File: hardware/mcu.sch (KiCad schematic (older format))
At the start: 51 parts, among them P3 CONN_01X08_DEBUG, P4 CONN_02X05_JTAG, P5 CONN_01X03_UART, P6 CONN_01X03_CAN, P7 CONN_01X05_ENCODER, SW2 SW_PUSH, U13 TM4C1294KCPDT, U14 74LVCH2T45, U15 SN65HVD231D, Y1 NX5032GA

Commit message: Gate driver layout mostly complete
- Gate driver layout
- Switch LM5102 for UCC27211 (higher current, more robust)
- Tweak gate drive circuit passives
- No soldermask on high-current traces
- Fix error in orientation of LAH-100P footprint
- Improved draft layout of control section
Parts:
- added C79: 1u, Capacitors_SMD:C_0603, symbol C
- added W22, W23: TEST_1P, symbol TEST_1P
- C32, C33: footprint Capacitors_SMD:C_0603 -> Capacitors_SMD:C_0805
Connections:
- net labels added: AIN_13, AIN_15, AIN_19, M0PWM0, T5CCP0
- net labels removed: AIN_0, AIN_3, GNDA, PWM6, PWM7
- wire segments 199 -> 197
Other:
- note added: "CONNECT JUMPER FOR\nFACTORY RESET ON\nNEXT SYSTEM RESET"
- note removed: "CONNECT TO ENABLE\nFACTORY RESET ON\nNEXT SYSTEM RESET"
- moved on the sheet: JP1, P5, R33, R57, R58, SW2, U13B

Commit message: All routing finished
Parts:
- removed P3: CONN_01X08_DEBUG, Pin_Headers:Pin_Header_Straight_1x08, symbol CONN_01X08
- added P3: CONN_01X09, Pin_Headers:Pin_Header_Straight_1x09, symbol CONN_01X09
- U14: footprint 2kwMotorController:VSSOP8 -> Housings_SSOP:MSOP-8_3x3mm_Pitch0.65mm
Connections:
- net labels added: VDDC
- wire segments 197 -> 200
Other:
- note removed: "REMOVE TO \nSET CAN ID"
- moved on the sheet: C32, C33, C34, C35, C36, C37, C38, C39, C40, C41, C42, C43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

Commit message: All DRC/ERC passed
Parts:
- removed W22, W23: TEST_1P, symbol TEST_1P
- added TP19, TP20, TP21, TP22, TP23: TEST_POINT, 2kwMotorController:TEST_PAD_1.27mm, symbol TEST_POINT
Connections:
- net CANH: now also TP21.1
- net CANL: now also TP22.1
- net CAN_RX: now also TP20.1
- net CAN_TX: now also TP19.1
- net VDDC: now also TP23.1

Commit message: tweaks, testpoints, decluttering
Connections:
- net FRST: now reaches JP1.1, U13.74 (PM4)
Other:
- moved on the sheet: JP1
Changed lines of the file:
@@
 L Jumper_NO_Small JP1
 U 1 1 59C1D74D
-P 5850 2300
-F 0 "JP1" H 5850 2380 50  0000 C CNN
-F 1 "Jumper_NO_Small" H 5860 2240 50  0001 C CNN
-F 2 "Pin_Headers:Pin_Header_Straight_1x02" H 5850 2300 50  0001 C CNN
-F 3 "" H 5850 2300 50  0000 C CNN
-	1    5850 2300
+P 4975 2300
+F 0 "JP1" H 4975 2380 50  0000 C CNN
+F 1 "Jumper_NO_Small" H 4985 2240 50  0001 C CNN
+F 2 "Pin_Headers:Pin_Header_Straight_1x02" H 4975 2300 50  0001 C CNN
+F 3 "" H 4975 2300 50  0000 C CNN
+	1    4975 2300
 	-1   0    0    -1
 $EndComp
@@
 L GND #PWR091
 U 1 1 59C1E162
-P 5700 2350
-F 0 "#PWR091" H 5700 2100 50  0001 C CNN
-F 1 "GND" H 5700 2200 50  0000 C CNN
-F 2 "" H 5700 2350 50  0000 C CNN
-F 3 "" H 5700 2350 50  0000 C CNN
-	1    5700 2350
+P 4825 2350
+F 0 "#PWR091" H 4825 2100 50  0001 C CNN
+F 1 "GND" H 4825 2200 50  0000 C CNN
+F 2 "" H 4825 2350 50  0000 C CNN
+F 3 "" H 4825 2350 50  0000 C CNN
+	1    4825 2350
 	-1   0    0    -1
 $EndComp
-Text Notes 5600 2550 2    60   ~ 0
+Text Notes 5975 2575 2    60   ~ 0
 CONNECT JUMPER FOR\nFACTORY RESET ON\nNEXT SYSTEM RESET
 $Comp
@@
 	8250 2700 8250 2650
 Wire Wire Line
-	8500 2700 8500 2650
+	8500 2650 8500 2700
 Connection ~ 8500 2650
 Wire Wire Line
-	8750 2700 8750 2650
+	8750 2650 8750 2700
 Connection ~ 8750 2650
 Wire Wire Line
@@
 Connection ~ 8500 3050
 Wire Wire Line
-	9000 2700 9000 2650
+	9000 2650 9000 2700
 Connection ~ 9000 2650
 Wire Wire Line
@@
 	3050 4800 3050 4700
 Wire Wire Line
-	6050 2300 5950 2300
-Wire Wire Line
-	5750 2300 5700 2300
-Wire Wire Line
-	5700 2300 5700 2350
+	6050 2300 5075 2300
+Wire Wire Line
+	4875 2300 4825 2300
+Wire Wire Line
+	4825 2300 4825 2350
 Wire Wire Line
 	4550 5150 4550 5250
@@
 Wire Wire Line
 	7900 2650 9450 2650
+Text Label 5600 2300 0    60   ~ 0
+FRST
 $EndSCHEMATC

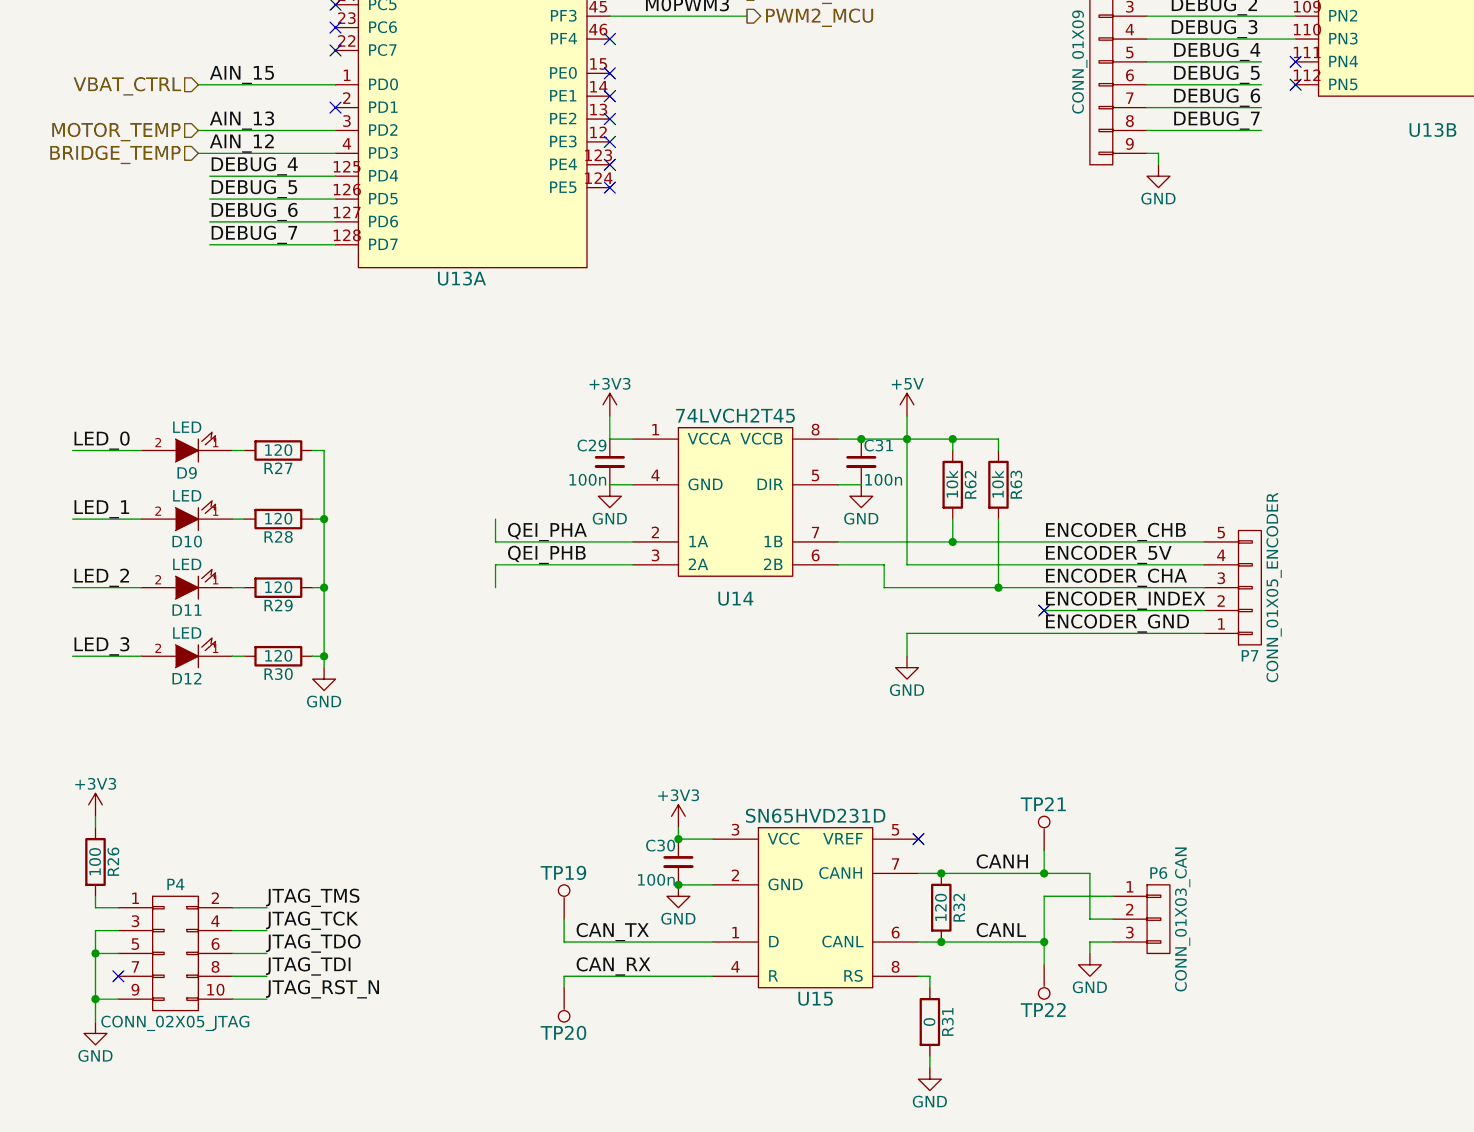
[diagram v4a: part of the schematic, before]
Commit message: Create and verify full Digikey BOM
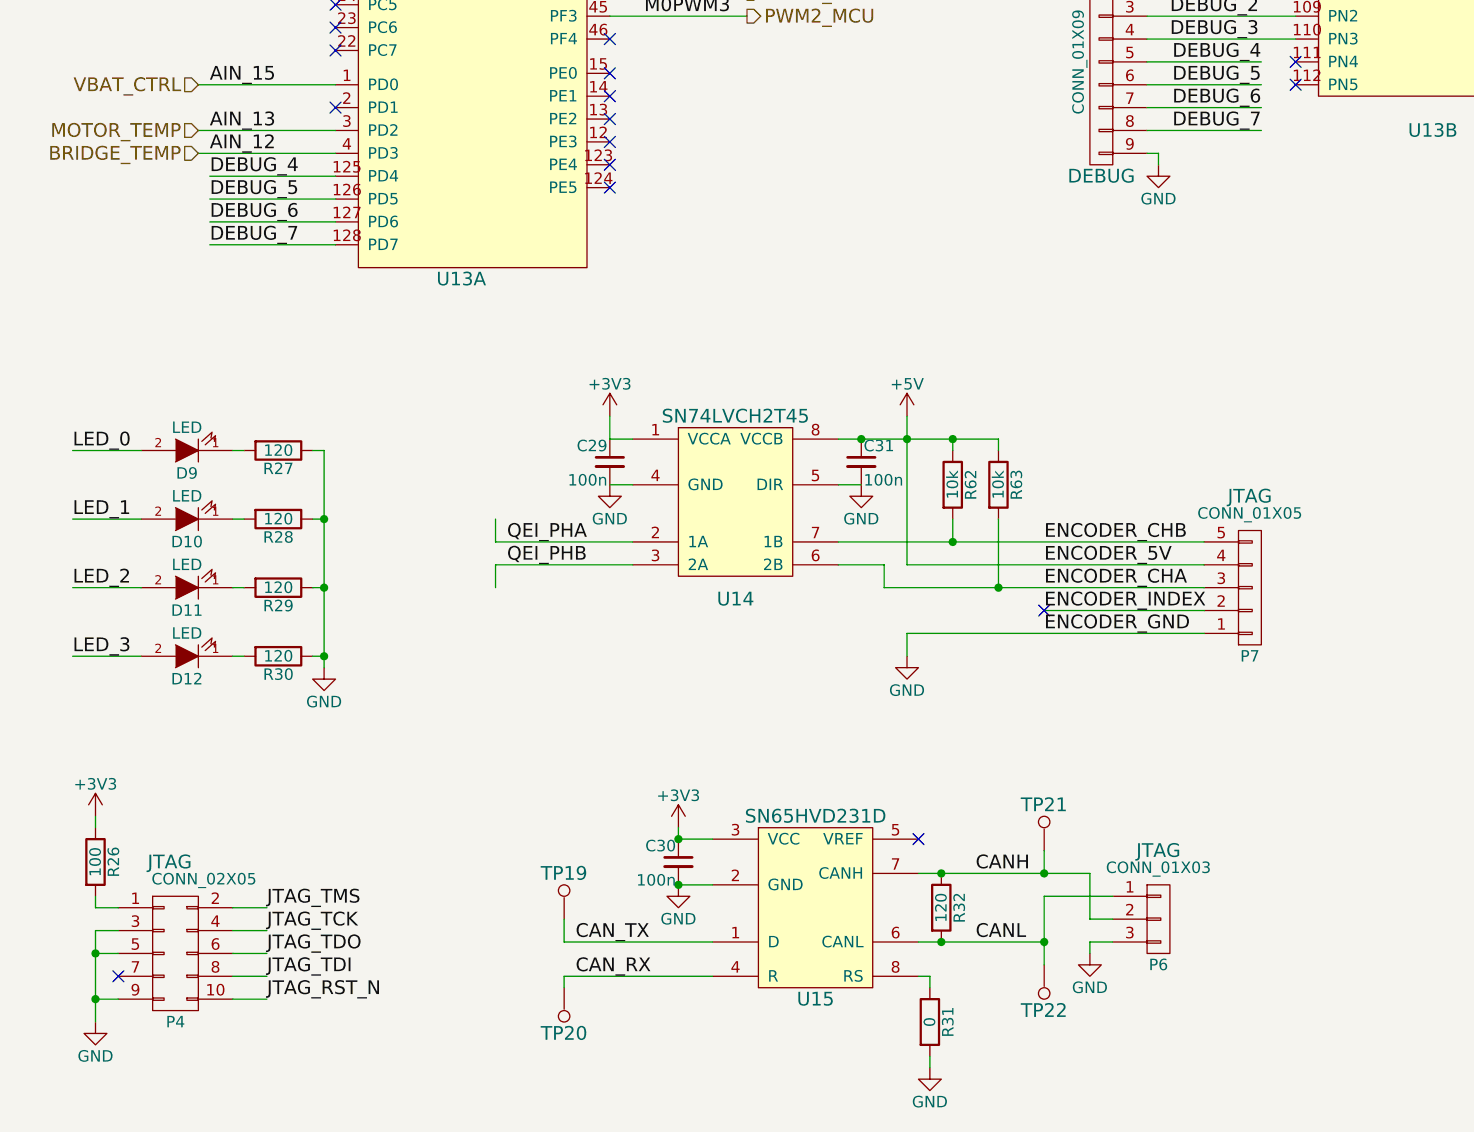
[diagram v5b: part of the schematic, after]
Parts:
- C29, C30, C31, C32, C33, C34, C35, C36, C37, C38, C39, C40, C41, C42, C43, C44, C45, C46, C47, C48, C49, C79: Voltage (none) -> 16V
- P3: Use (none) -> DEBUG
- P4: value CONN_02X05_JTAG -> CONN_02X05; Use (none) -> JTAG
- P6: value CONN_01X03_CAN -> CONN_01X03; Use (none) -> JTAG
- P7: value CONN_01X05_ENCODER -> CONN_01X05; Use (none) -> JTAG
- U14: value 74LVCH2T45 -> SN74LVCH2T45
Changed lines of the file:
@@
 F 2 "Capacitors_SMD:C_0603" H 8788 2700 50  0001 C CNN
 F 3 "" H 8750 2850 50  0000 C CNN
+F 4 "16V" H 8750 2850 60  0001 C CNN "Voltage"
 	1    8750 2850
 	1    0    0    -1
@@
 F 2 "Capacitors_SMD:C_0603" H 8538 2700 50  0001 C CNN
 F 3 "" H 8500 2850 50  0000 C CNN
+F 4 "16V" H 8500 2850 60  0001 C CNN "Voltage"
 	1    8500 2850
 	1    0    0    -1
@@
 F 2 "Capacitors_SMD:C_0603" H 8288 2700 50  0001 C CNN
 F 3 "" H 8250 2850 50  0000 C CNN
+F 4 "16V" H 8250 2850 60  0001 C CNN "Voltage"
 	1    8250 2850
 	1    0    0    -1
@@
 F 2 "Capacitors_SMD:C_0603" H 9038 2700 50  0001 C CNN
 F 3 "" H 9000 2850 50  0000 C CNN
+F 4 "16V" H 9000 2850 60  0001 C CNN "Voltage"
 	1    9000 2850
 	1    0    0    -1
@@
 F 2 "Capacitors_SMD:C_0603" H 9138 1100 50  0001 C CNN
 F 3 "" H 9100 1250 50  0000 C CNN
+F 4 "16V" H 9100 1250 60  0001 C CNN "Voltage"
 	1    9100 1250
 	1    0    0    -1
@@
 F 2 "Capacitors_SMD:C_0603" H 8888 1100 50  0001 C CNN
 F 3 "" H 8850 1250 50  0000 C CNN
+F 4 "16V" H 8850 1250 60  0001 C CNN "Voltage"
 	1    8850 1250
 	1    0    0    -1
@@
 F 2 "Capacitors_SMD:C_0603" H 8638 1100 50  0001 C CNN
 F 3 "" H 8600 1250 50  0000 C CNN
+F 4 "16V" H 8600 1250 60  0001 C CNN "Voltage"
 	1    8600 1250
 	1    0    0    -1
@@
 F 2 "Capacitors_SMD:C_0603" H 8388 1100 50  0001 C CNN
 F 3 "" H 8350 1250 50  0000 C CNN
+F 4 "16V" H 8350 1250 60  0001 C CNN "Voltage"
 	1    8350 1250
 	1    0    0    -1
@@
 F 2 "Capacitors_SMD:C_0603" H 9138 1800 50  0001 C CNN
 F 3 "" H 9100 1950 50  0000 C CNN
+F 4 "16V" H 9100 1950 60  0001 C CNN "Voltage"
 	1    9100 1950
 	1    0    0    -1
@@
 F 2 "Capacitors_SMD:C_0603" H 8888 1800 50  0001 C CNN
 F 3 "" H 8850 1950 50  0000 C CNN
+F 4 "16V" H 8850 1950 60  0001 C CNN "Voltage"
 	1    8850 1950
 	1    0    0    -1
@@
 F 2 "Capacitors_SMD:C_0603" H 8638 1800 50  0001 C CNN
 F 3 "" H 8600 1950 50  0000 C CNN
+F 4 "16V" H 8600 1950 60  0001 C CNN "Voltage"
 	1    8600 1950
 	1    0    0    -1
@@
 F 2 "Capacitors_SMD:C_0603" H 8388 1800 50  0001 C CNN
 F 3 "" H 8350 1950 50  0000 C CNN
+F 4 "16V" H 8350 1950 60  0001 C CNN "Voltage"
 	1    8350 1950
 	1    0    0    -1
@@
 F 2 "Capacitors_SMD:C_0805" H 8138 1100 50  0001 C CNN
 F 3 "" H 8100 1250 50  0000 C CNN
+F 4 "16V" H 8100 1250 60  0001 C CNN "Voltage"
 	1    8100 1250
 	1    0    0    -1
@@
 F 2 "Capacitors_SMD:C_0805" H 8138 1800 50  0001 C CNN
 F 3 "" H 8100 1950 50  0000 C CNN
+F 4 "16V" H 8100 1950 60  0001 C CNN "Voltage"
 	1    8100 1950
 	1    0    0    -1
@@
 F 2 "Capacitors_SMD:C_0603" H 10188 5800 50  0001 C CNN
 F 3 "" H 10150 5950 50  0000 C CNN
+F 4 "16V" H 10150 5950 60  0001 C CNN "Voltage"
 	1    10150 5950
 	1    0    0    -1
@@
 F 2 "Capacitors_SMD:C_0603" H 10588 5800 50  0001 C CNN
 F 3 "" H 10550 5950 50  0000 C CNN
+F 4 "16V" H 10550 5950 60  0001 C CNN "Voltage"
 	1    10550 5950
 	1    0    0    -1
@@
 U 1 1 59A6BA60
 P 1150 7050
-F 0 "P4" H 1150 7350 50  0000 C CNN
-F 1 "CONN_02X05_JTAG" H 1150 6750 50  0000 C CNN
+F 0 "P4" H 1150 6750 50  0000 C CNN
+F 1 "CONN_02X05" H 1275 7375 50  0000 C CNN
 F 2 "Pin_Headers:Pin_Header_Straight_2x05_Pitch1.27mm" H 1150 5850 50  0001 C CNN
 F 3 "" H 1150 5850 50  0000 C CNN
+F 4 "JTAG" H 1125 7450 60  0000 C CNN "Use"
 	1    1150 7050
 	1    0    0    -1
@@
 F 2 "Capacitors_SMD:C_0603" H 11038 2350 50  0001 C CNN
 F 3 "" H 11000 2500 50  0000 C CNN
+F 4 "16V" H 11000 2500 60  0001 C CNN "Voltage"
 	1    11000 2500
 	1    0    0    -1
@@
 F 2 "Capacitors_SMD:C_0603" H 10788 2350 50  0001 C CNN
 F 3 "" H 10750 2500 50  0000 C CNN
+F 4 "16V" H 10750 2500 60  0001 C CNN "Voltage"
 	1    10750 2500
 	1    0    0    -1
@@
 F 2 "Capacitors_SMD:C_0603" H 3350 6650 50  0001 C CNN
 F 3 "" H 3350 6650 50  0000 C CNN
+F 4 "16V" H 3350 6650 60  0001 C CNN "Voltage"
 	1    3350 6650
 	-1   0    0    -1
@@
 P 5850 5450
 F 0 "P7" H 5850 5750 50  0000 C CNN
-F 1 "CONN_01X05_ENCODER" V 5950 5450 50  0000 C CNN
+F 1 "CONN_01X05" H 5850 5125 50  0000 C CNN
 F 2 "2kwMotorController:TERM_5P_2-5_1990038" H 5850 5450 50  0001 C CNN
 F 3 "" H 5850 5450 50  0000 C CNN
+F 4 "JTAG" H 5850 5050 60  0000 C CNN "Use"
 	1    5850 5450
 	1    0    0    1
@@
 U 1 1 59C7E31D
 P 5450 6900
-F 0 "P6" H 5450 7100 50  0000 C CNN
-F 1 "CONN_01X03_CAN" V 5550 6900 50  0000 C CNN
+F 0 "P6" H 5450 6700 50  0000 C CNN
+F 1 "CONN_01X03" H 5450 7125 50  0000 C CNN
 F 2 "2kwMotorController:TERM_3P_2-5_1990012" H 5450 6900 50  0001 C CNN
 F 3 "" H 5450 6900 50  0000 C CNN
+F 4 "JTAG" H 5450 7200 60  0000 C CNN "Use"
 	1    5450 6900
 	1    0    0    -1
@@
 P 3600 5100
 F 0 "U14" H 3600 4700 60  0000 C CNN
-F 1 "74LVCH2T45" H 3600 5500 60  0000 C CNN
+F 1 "SN74LVCH2T45" H 3600 5500 60  0000 C CNN
 F 2 "Housings_SSOP:MSOP-8_3x3mm_Pitch0.65mm" H 3600 5100 60  0001 C CNN
 F 3 "" H 3600 5100 60  0000 C CNN
@@
 F 2 "Capacitors_SMD:C_0603" H 4150 4900 50  0001 C CNN
 F 3 "" H 4150 4900 50  0000 C CNN
+F 4 "16V" H 4150 4900 60  0001 C CNN "Voltage"
 	1    4150 4900
 	1    0    0    -1
@@
 F 2 "Capacitors_SMD:C_0603" H 3050 4900 50  0001 C CNN
 F 3 "" H 3050 4900 50  0000 C CNN
+F 4 "16V" H 3050 4900 60  0001 C CNN "Voltage"
 	1    3050 4900
 	-1   0    0    -1
@@
 F 2 "Capacitors_SMD:C_0603" H 8088 5100 50  0001 C CNN
 F 3 "" H 8050 5250 50  0000 C CNN
+F 4 "16V" H 8050 5250 60  0001 C CNN "Voltage"
 	1    8050 5250
 	1    0    0    -1
@@
 F 2 "Pin_Headers:Pin_Header_Straight_1x09" H 5200 3150 50  0001 C CNN
 F 3 "" H 5200 3150 50  0000 C CNN
+F 4 "DEBUG" H 5200 2650 60  0000 C CNN "Use"
 	1    5200 3150
 	-1   0    0    -1

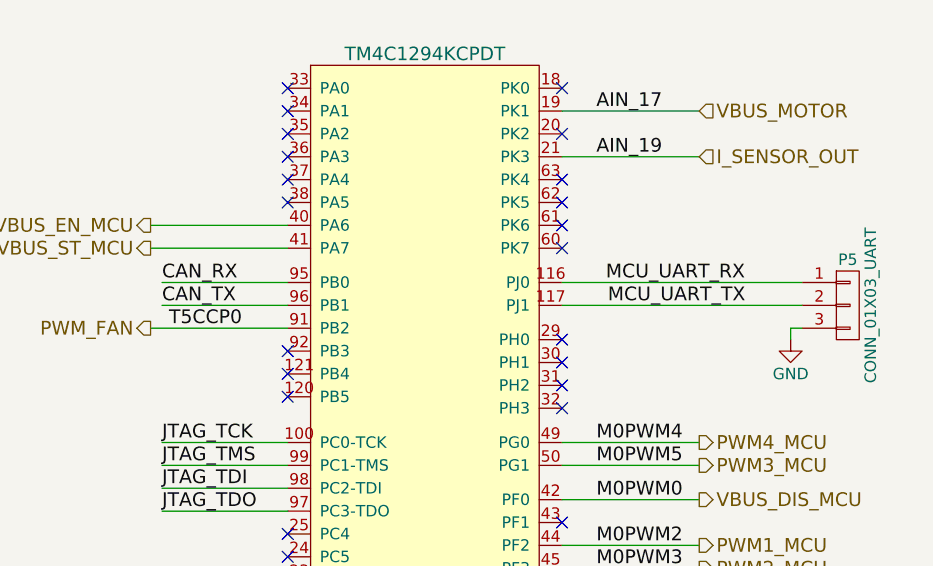
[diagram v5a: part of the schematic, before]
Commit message: Firmware started; logging task finished
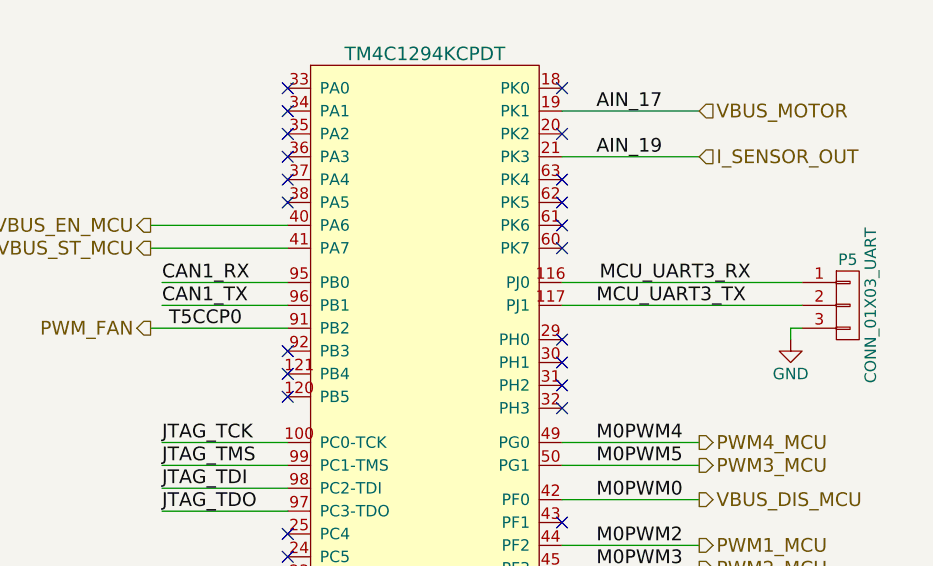
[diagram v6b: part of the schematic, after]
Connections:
- net CAN_RX: no longer U13.95 (PB0)
- net CAN_TX: no longer U13.96 (PB1)
- net MCU_UART_RX renamed MCU_UART3_RX
- net MCU_UART_TX renamed MCU_UART3_TX
- new net CAN1_RX: U13.95 (PB0)
- new net CAN1_TX: U13.96 (PB1)
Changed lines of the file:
@@
 NoConn ~ 8500 5550
 Text Label 1300 1700 0    60   ~ 0
-CAN_RX
+CAN1_RX
 Text Label 1300 1800 0    60   ~ 0
-CAN_TX
+CAN1_TX
 $Comp
 L R R32
@@
 Text HLabel 1250 1450 0    60   Output ~ 0
 VBUS_EN_MCU
-Text Label 3850 1700 2    60   ~ 0
-MCU_UART_RX
-Text Label 3250 1800 0    60   ~ 0
-MCU_UART_TX
+Text Label 3875 1700 2    60   ~ 0
+MCU_UART3_RX
+Text Label 3200 1800 0    60   ~ 0
+MCU_UART3_TX
 $Comp
 L CONN_01X03 P5

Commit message: Open Loop Test Code
Rough version of control task for open loop testing of H-bridge
Rough version of sensor code
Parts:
- D10, D11, D12, D9: symbol LED -> LED-RESCUE-2kwMotorController
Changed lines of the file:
@@
 EESchema Schematic File Version 2
+LIBS:2kwMotorController-rescue
 LIBS:power
 LIBS:device
@@
 LED_3
 $Comp
-L LED D9
+L LED-RESCUE-2kwMotorController D9
 U 1 1 59C4E560
 P 1200 4850
@@
 $EndComp
 $Comp
-L LED D10
+L LED-RESCUE-2kwMotorController D10
 U 1 1 59C4FA15
 P 1200 5150
@@
 $EndComp
 $Comp
-L LED D11
+L LED-RESCUE-2kwMotorController D11
 U 1 1 59C4FE16
 P 1200 5450
@@
 $EndComp
 $Comp
-L LED D12
+L LED-RESCUE-2kwMotorController D12
 U 1 1 59C4FE24
 P 1200 5750

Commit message: Revised layout mostly complete
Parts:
- removed D10, D11, D12, D9: LED, LEDs:LED_0603, symbol LED-RESCUE-2kwMotorController
- removed R30: 120, Resistors_SMD:R_0603, symbol R
- added C85, C86: 100n, Capacitors_SMD:C_0603, symbol C_Small
- added JP2: Jumper_NO_Small, Pin_Headers:Pin_Header_Straight_1x02, symbol Jumper_NO_Small
- added P15: CONN_01X04, Pin_Headers:Pin_Header_Straight_1x04, symbol CONN_01X04
- added R39: 10k, Resistors_SMD:R_0603, symbol R
- added U22: SN74LVCH2T45, Housings_SSOP:MSOP-8_3x3mm_Pitch0.65mm, symbol 74LVCH2T45
- P6: footprint 2kwMotorController:TERM_3P_2-5_1990012 -> Pin_Headers:Pin_Header_Straight_1x03
- P7: footprint 2kwMotorController:TERM_5P_2-5_1990038 -> Pin_Headers:Pin_Header_Straight_1x05
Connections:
- net CAN_RX is gone; now on net CAN1_RX: TP20.1, U15.4 (R)
- net CAN_TX is gone; now on net CAN1_TX: TP19.1, U15.1 (D)
- net +3V3: now also C85.1, U22.1 (VCCA)
- net +5V: now also C86.1, R39.2, U22.8 (VCCB)
- net CANH: now also R32.2; no longer R32.1
- net CANL: now also JP2.2; no longer R32.2
- net ENCODER_INDEX: now also R39.1, U22.7 (1B)
- net GND: now also C85.2, C86.2, P15.4 (P4), U22.4 (GND), U22.5 (DIR), U22.6 (2B); no longer R27.1, R28.1, R29.1
- net LED_0: now also R27.2
- net LED_1: now also R28.2
- net LED_2: now also R29.2
- net QEI_IDX: now also U22.2 (1A)
- net LED_3: no longer names the net of U13.106 (PP5)
- new net: JP2.1, R32.1
- new net BLUE: P15.3 (P3), R29.1
- new net GREEN: P15.2 (P2), R28.1
- new net RED: P15.1 (P1), R27.1
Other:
- moved on the sheet: C29, C30, C31, C46, C47, C79, P6, P7, R27, R28, R29, R31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
